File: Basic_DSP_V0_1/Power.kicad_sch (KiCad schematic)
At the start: 26 parts, among them J1 53048-0310, U3 TLV76733QWDRBRQ1, U4 NCP718ASN180T1G, U5 NCP718BSN500T1G

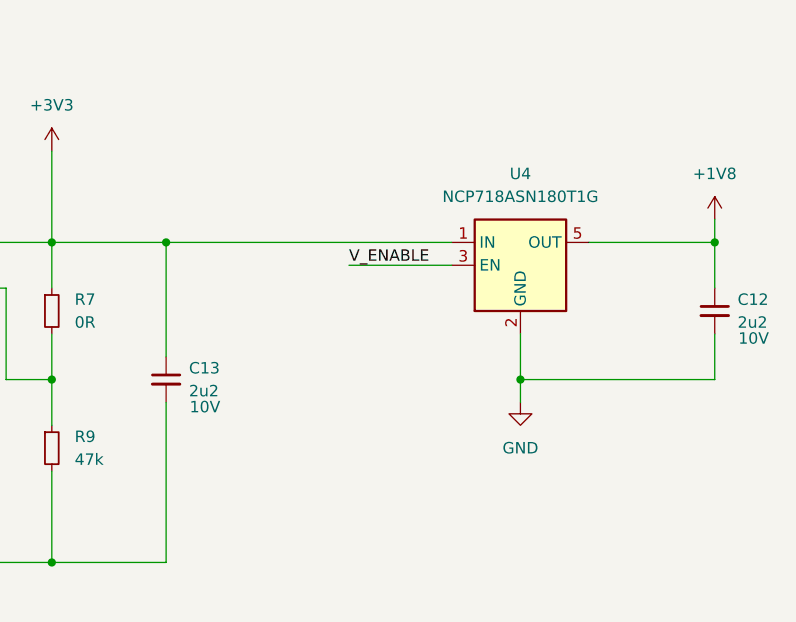
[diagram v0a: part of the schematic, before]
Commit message: Updates to basic DSP schematic
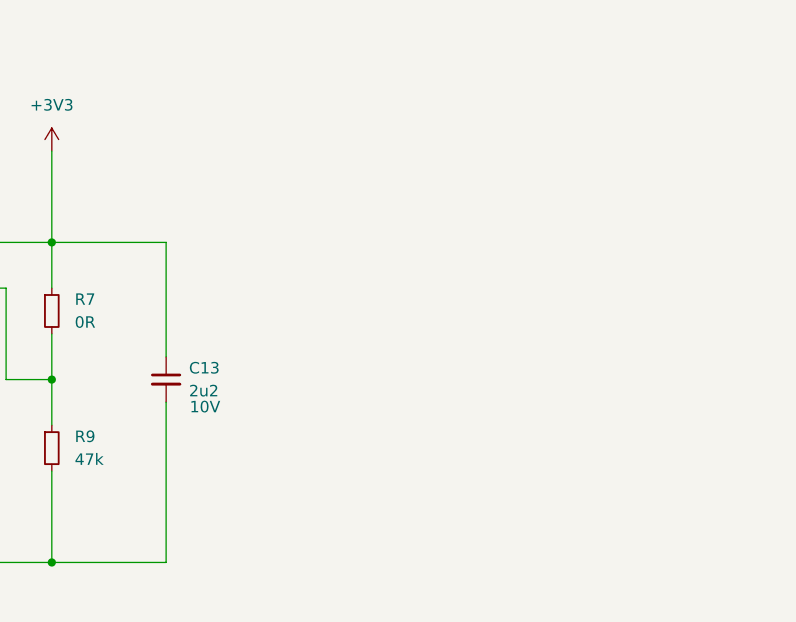
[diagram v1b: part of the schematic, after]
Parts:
- removed C12: 2u2, Capacitor_SMD:C_0402_1005Metric, symbol Device:C_Small
- removed U4: NCP718ASN180T1G, Package_TO_SOT_SMD:SOT-23-5, symbol Regulator_Linear:NCP718xSN500

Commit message: Minor updates to Basic schematic
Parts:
- C13, C14: footprint Capacitor_SMD:C_0402_1005Metric -> Capacitor_SMD:C_0603_1608Metric_Pad1.08x0.95mm_HandSolder
- R10, R7, R8, R9: footprint Resistor_SMD:R_0402_1005Metric_Pad0.72x0.64mm_HandSolder -> Resistor_SMD:R_0603_1608Metric_Pad0.98x0.95mm_HandSolder
- R11: footprint Resistor_SMD:R_0805_2012Metric_Pad1.20x1.40mm_HandSolder -> Resistor_SMD:R_0603_1608Metric_Pad0.98x0.95mm_HandSolder
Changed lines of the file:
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@@
 			)
 		)
-		(property "Footprint" "Capacitor_SMD:C_0402_1005Metric"
+		(property "Footprint" "Capacitor_SMD:C_0603_1608Metric_Pad1.08x0.95mm_HandSolder"
 			(at 199.39 106.68 0)
 			(effects
@@
 			)
 		)
-		(property "Footprint" "Resistor_SMD:R_0402_1005Metric_Pad0.72x0.64mm_HandSolder"
+		(property "Footprint" "Resistor_SMD:R_0603_1608Metric_Pad0.98x0.95mm_HandSolder"
 			(at 186.69 88.9 0)
 			(effects
@@
 			)
 		)
-		(property "Footprint" "Resistor_SMD:R_0402_1005Metric_Pad0.72x0.64mm_HandSolder"
+		(property "Footprint" "Resistor_SMD:R_0603_1608Metric_Pad0.98x0.95mm_HandSolder"
 			(at 275.59 102.87 0)
 			(effects
@@
 			)
 		)
-		(property "Footprint" "Resistor_SMD:R_0805_2012Metric_Pad1.20x1.40mm_HandSolder"
+		(property "Footprint" "Resistor_SMD:R_0603_1608Metric_Pad0.98x0.95mm_HandSolder"
 			(at 227.33 184.15 0)
 			(effects
@@
 			)
 		)
-		(property "Footprint" "Capacitor_SMD:C_0402_1005Metric"
+		(property "Footprint" "Capacitor_SMD:C_0603_1608Metric_Pad1.08x0.95mm_HandSolder"
 			(at 288.29 95.25 0)
 			(effects
@@
 			)
 		)
-		(property "Footprint" "Resistor_SMD:R_0402_1005Metric_Pad0.72x0.64mm_HandSolder"
+		(property "Footprint" "Resistor_SMD:R_0603_1608Metric_Pad0.98x0.95mm_HandSolder"
 			(at 275.59 87.63 0)
 			(effects
@@
 			)
 		)
-		(property "Footprint" "Resistor_SMD:R_0402_1005Metric_Pad0.72x0.64mm_HandSolder"
+		(property "Footprint" "Resistor_SMD:R_0603_1608Metric_Pad0.98x0.95mm_HandSolder"
 			(at 186.69 106.68 0)
 			(effects

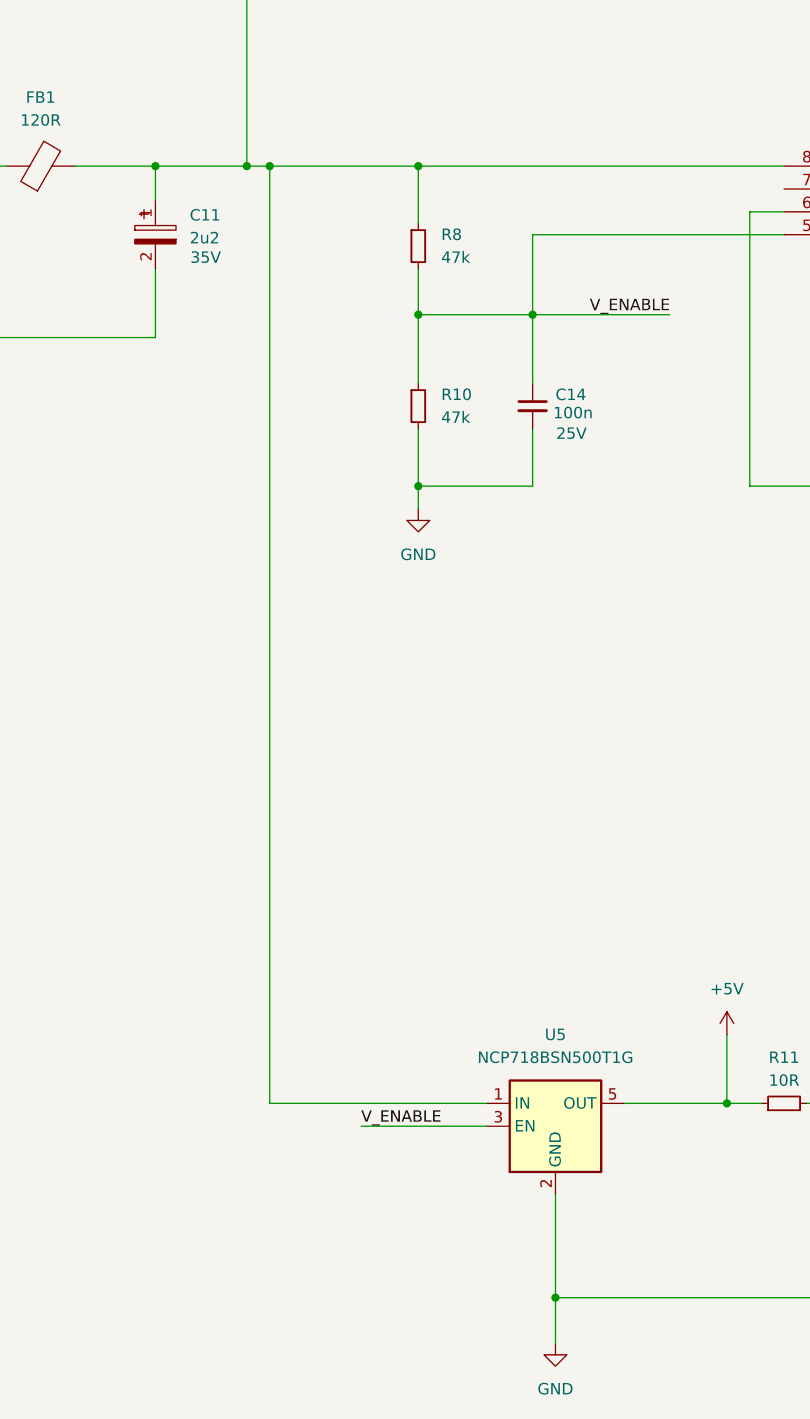
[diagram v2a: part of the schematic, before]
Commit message: Started layout
Removed library from repo as it was messin with the links
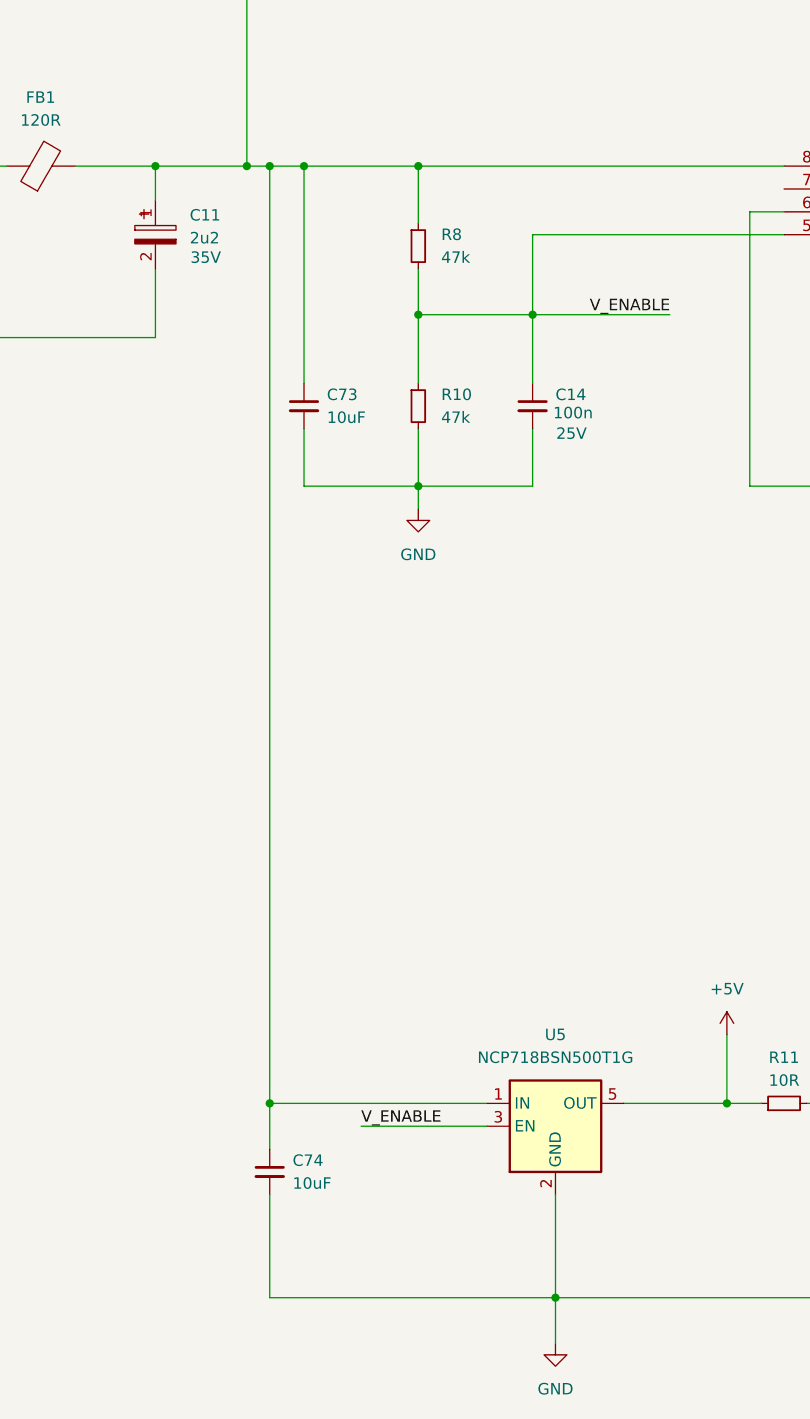
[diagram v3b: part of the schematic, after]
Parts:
- added C73, C74: 10uF, Capacitor_SMD:C_0603_1608Metric, symbol Device:C_Small
- J1: footprint (none) -> Chase_Conn:SHDRRA3W35P0X125_1X3_550X550X350P
- U3: footprint (none) -> Chase_LDO:SON65P300X300X100-9N-D
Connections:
- net GND: now also C73.2, C74.2
- net at C11.1, D1.1 (K), FB1.2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: now also C73.1, C74.1

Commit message: Basic placement on PCB
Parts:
- removed C16, C17, C18, C19, C20, C21, C22: 22u, Capacitor_SMD:C_1210_3225Metric, symbol Device:C_Small

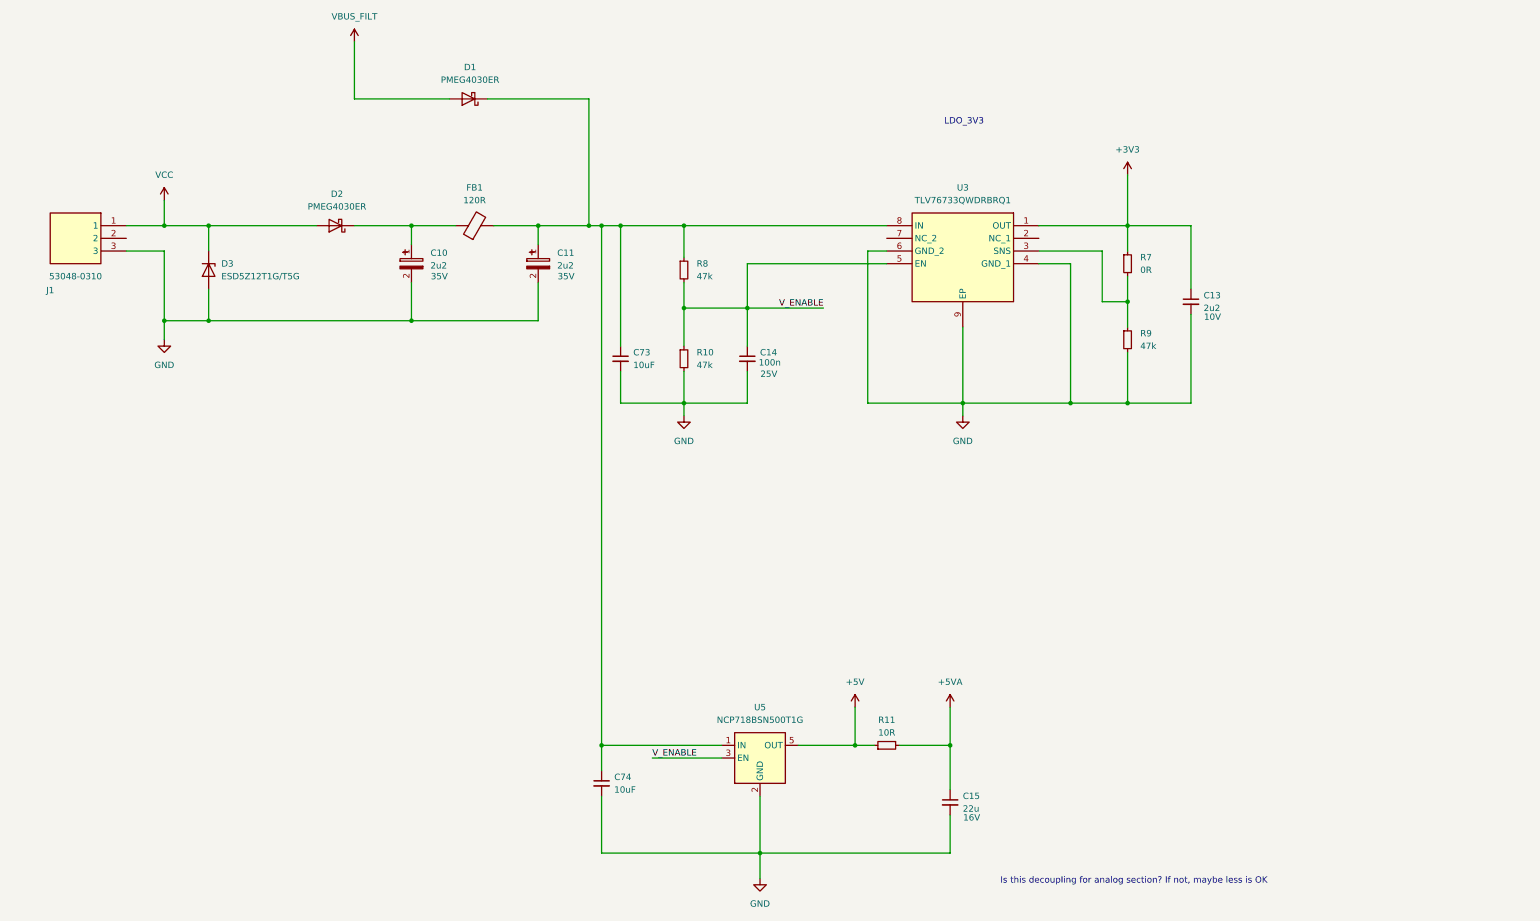
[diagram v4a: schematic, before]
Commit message: Updated parts with LCSC order codes
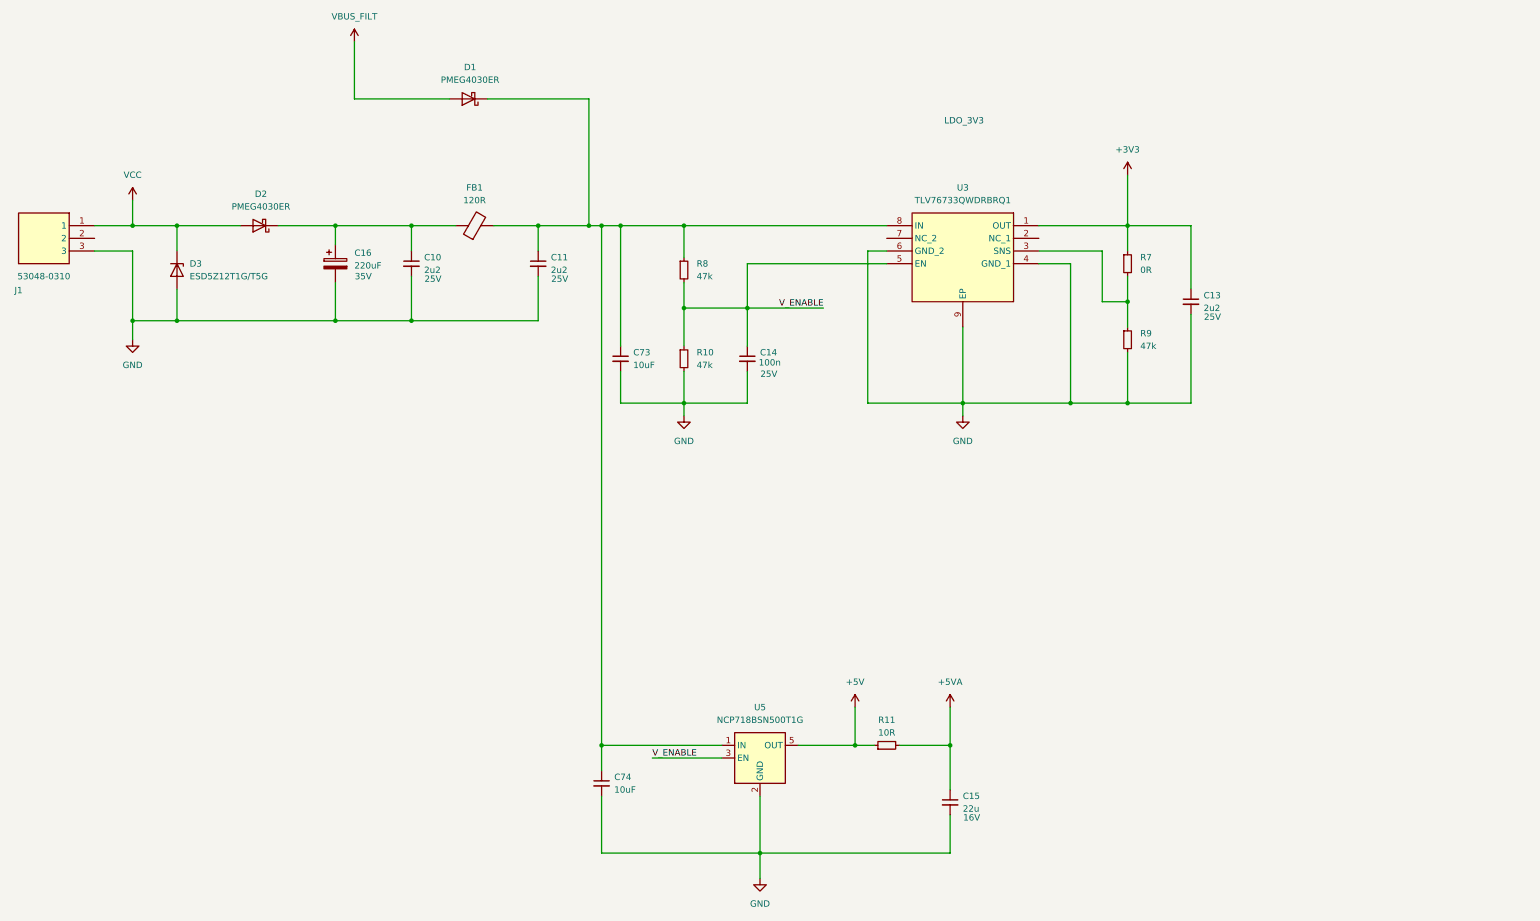
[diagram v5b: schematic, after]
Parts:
- removed C10, C11: 2u2, Chase_Capacitor:CAPAE430X550N, symbol Chase_Capacitor:865250540001
- added C10, C11: 2u2, Capacitor_SMD:C_0603_1608Metric_Pad1.08x0.95mm_HandSolder, symbol Device:C_Small
- added C16: 220uF, Capacitor_SMD:CP_Elec_8x10.5, symbol Device:C_Polarized
- C13: MF Murata Electronics -> FH (Guangdong Fenghua Advanced Tech); MPN GRM155Z71A225KE01D -> 0603B225K250NT; OC_LCSC (none) -> C99228; Voltage 10V -> 25V
- C14: MF TAIYO YUDEN -> FH (Guangdong Fenghua Advanced Tech); MPN MBAST105SB7104KFNA01 -> 0603B104M250NT; OC_LCSC (none) -> C336628
- C15: footprint Capacitor_SMD:C_1210_3225Metric -> Capacitor_SMD:C_0603_1608Metric_Pad1.08x0.95mm_HandSolder; MF Samsung Electro-Mechanics -> HRE; MPN CL32B226MOJNNNE -> CGA0603X5R226M160JT; OC_LCSC (none) -> C6119868
- C73, C74: MF KYOCERA AVX -> Samsung Electro-Mechanics; MPN 06033D106MAT2A -> CL10A106MA8NRNC; OC_LCSC (none) -> C96446
- D1, D2: MF (none) -> Shikues; MPN (none) -> PMEG4030ER; OC_LCSC (none) -> C5366303
- D3: MF (none) -> FUXINSEMI; MPN (none) -> ESD5Z12T1G; OC_LCSC (none) -> C7436544; Voltage (none) -> 12V
- FB1: OC_LCSC (none) -> C85831
- J1: MF (none) -> MOLEX; MPN (none) -> 530480310; OC_LCSC (none) -> C505275
- R10, R8, R9: MF (none) -> YAGEO; MPN (none) -> RC0603FR-0747KL; OC_LCSC (none) -> C105579
- R11: MF (none) -> UNI-ROYAL(Uniroyal Elec); MPN (none) -> 0603WAF100JT5E; OC_LCSC (none) -> C22859
- R7: MF (none) -> UNI-ROYAL(Uniroyal Elec); MPN (none) -> 0603WAF0000T5E; OC_LCSC (none) -> C21189
- U3: MF (none) -> Texas Instruments; MPN (none) -> TLV76733QWDRBRQ1; OC_LCSC (none) -> C5220143
- U5: MF (none) -> onsemi; MPN (none) -> NCP718BSN500T1G; OC_LCSC (none) -> C892796
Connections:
- net GND: now also C10.2, C11.2, C16.2
- net at C73.1, C74.1, D1.1 (K)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: now also C11.1
- net at D2.1 (K), FB1.1: now also C10.1, C16.1
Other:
- note removed: "Is this decoupling for analog section? If not, maybe less is OK"
- moved on the sheet: D2, D3, J1

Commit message: Layout and removal of PDN ferrites
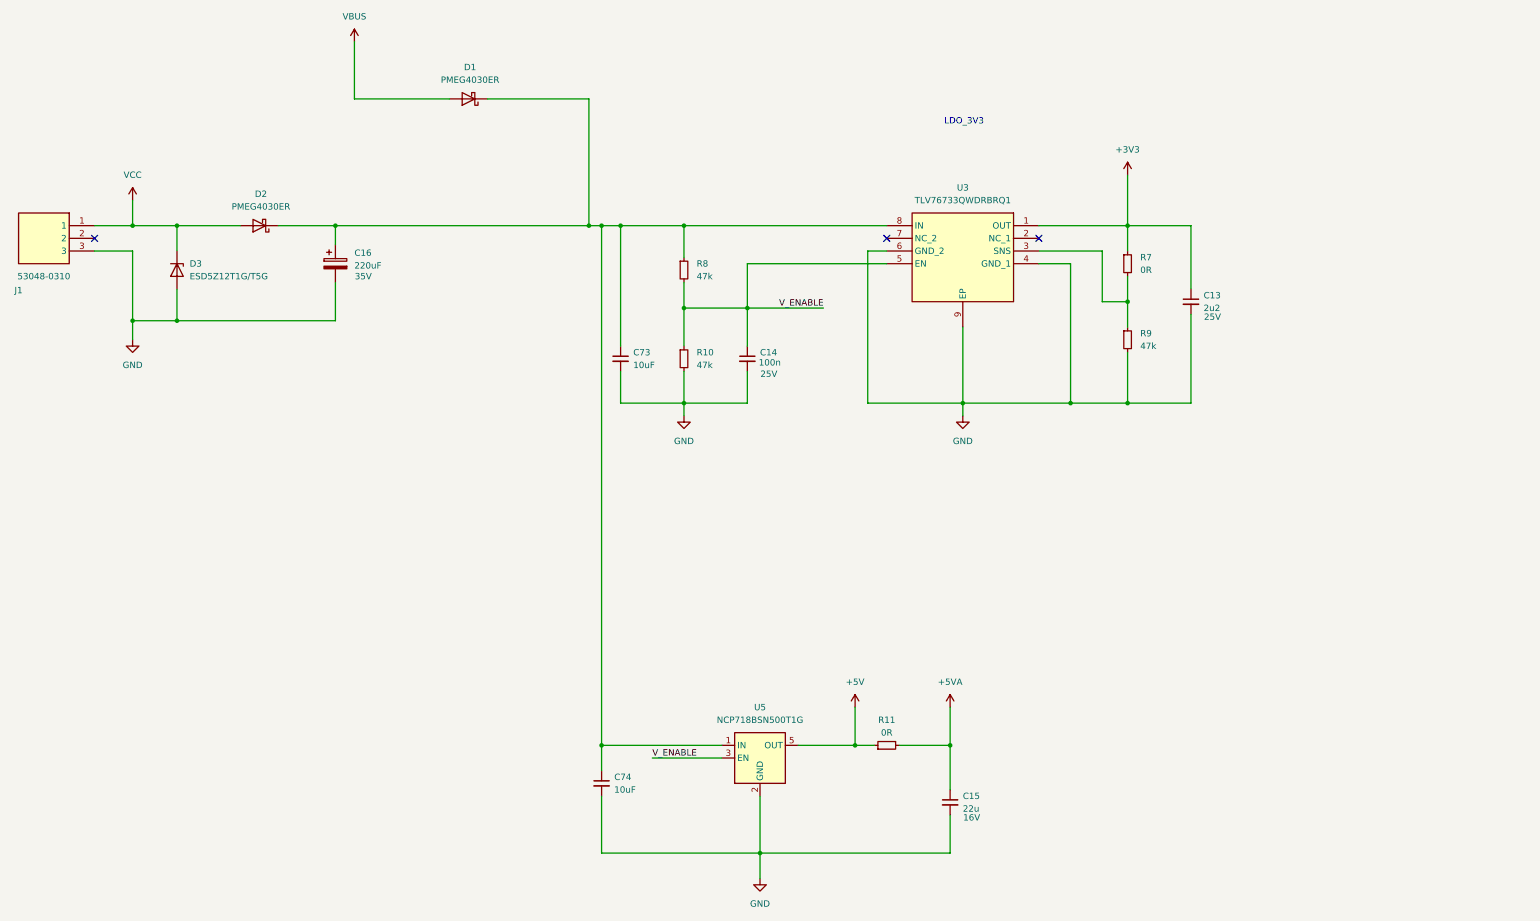
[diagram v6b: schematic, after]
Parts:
- removed C10, C11: 2u2, Capacitor_SMD:C_0603_1608Metric_Pad1.08x0.95mm_HandSolder, symbol Device:C_Small
- removed FB1: 120R, Inductor_SMD:L_0603_1608Metric, symbol Device:FerriteBead
- R11: value 10R -> 0R
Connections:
- net at C73.1, C74.1, D1.1 (K)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: now also C16.1, D2.1 (K)
- net VBUS_FILT renamed VBUS
- no-connect marks 0 -> 3
